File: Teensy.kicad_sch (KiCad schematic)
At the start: 8 parts

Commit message: test commit
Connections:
- net Servo_Pin1_1: now also Q100.24
- net Servo_Pin2_1: now also Q100.25
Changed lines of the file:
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@@
+	(wire
+		(pts
+			(xy 93.98 106.68) (xy 116.84 106.68)
+		)
+		(stroke
+			(width 0)
+			(type default)
+		)
+	)
 	(wire
 		(pts
@@
 		)
 		(stroke
+			(width 0)
+			(type default)
+		)
+	)
+	(wire
+		(pts
+			(xy 93.98 104.14) (xy 116.84 104.14)
+		)
+		(stroke

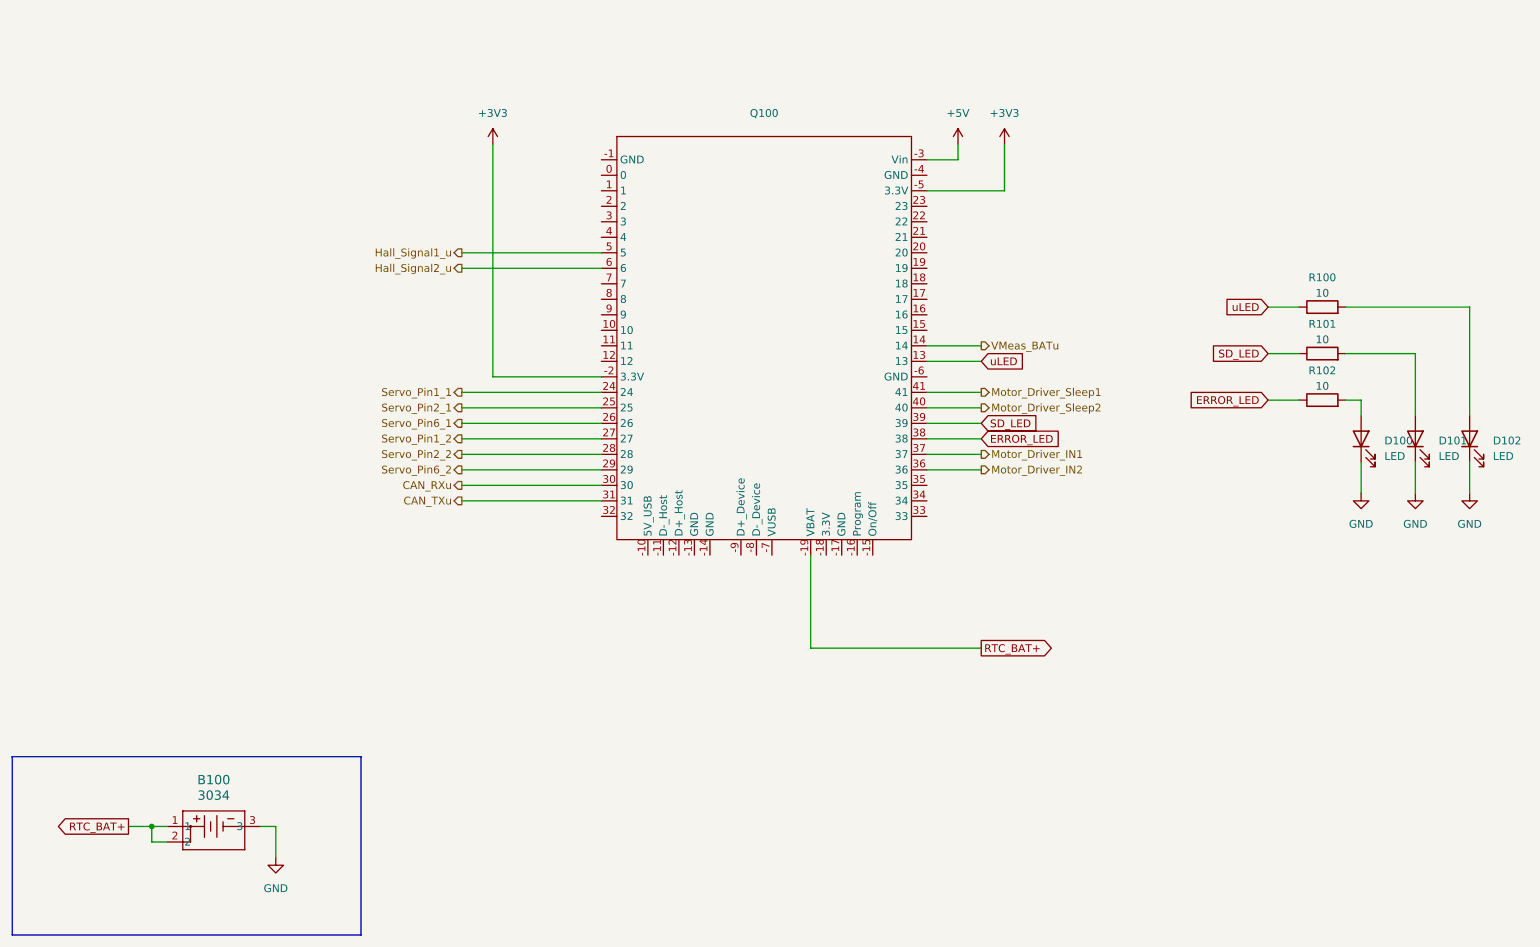
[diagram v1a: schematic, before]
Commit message: Added gyro, current sense, removed servo control, added temp sense
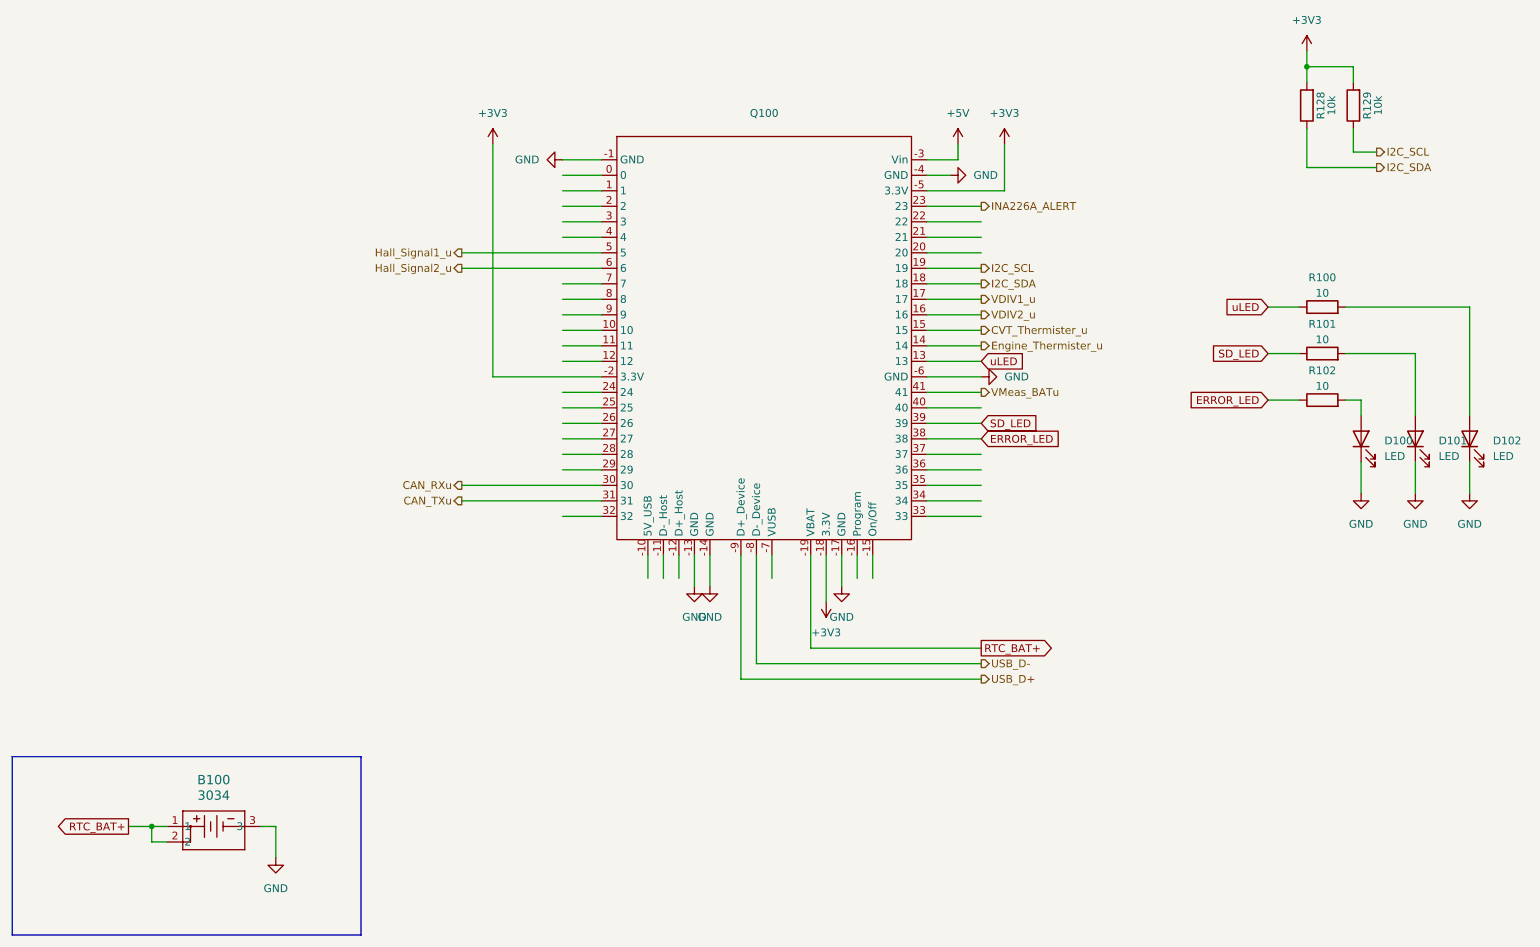
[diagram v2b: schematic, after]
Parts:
- added R128, R129: 10k, Resistor_SMD:R_0603_1608Metric_Pad0.98x0.95mm_HandSolder, symbol Device:R
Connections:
- net Motor_Driver_Sleep1 is gone; now on net VMeas_BATu: Q100.41
- net +3V3: now also Q100.-18 (3.3V), R128.2, R129.2
- net GND: now also Q100.-1 (GND), Q100.-13 (GND), Q100.-14 (GND), Q100.-17 (GND), Q100.-4 (GND), Q100.-6 (GND)
- net VMeas_BATu: no longer Q100.14
- net USB_D-: now reaches Q100.-8 (D-_Device)
- net USB_D+: now reaches Q100.-9 (D+_Device)
- net CVT_Thermister_u: now reaches Q100.15
- net VDIV2_u: now reaches Q100.16
- net VDIV1_u: now reaches Q100.17
- net I2C_SDA: now reaches Q100.18
- net I2C_SDA: now also R128.1
- net I2C_SCL: now reaches Q100.19
- net I2C_SCL: now also R129.1
- net INA226A_ALERT: now reaches Q100.23
- net Motor_Driver_IN1: no longer names the net of Q100.37
- net Motor_Driver_IN2: no longer names the net of Q100.36
- net Motor_Driver_Sleep2: no longer names the net of Q100.40
- net Servo_Pin1_1: no longer names the net of Q100.24
- net Servo_Pin1_2: no longer names the net of Q100.27
- net Servo_Pin2_1: no longer names the net of Q100.25
- net Servo_Pin2_2: no longer names the net of Q100.28
- net Servo_Pin6_1: no longer names the net of Q100.26
- net Servo_Pin6_2: no longer names the net of Q100.29
- new net Engine_Thermister_u: Q100.14

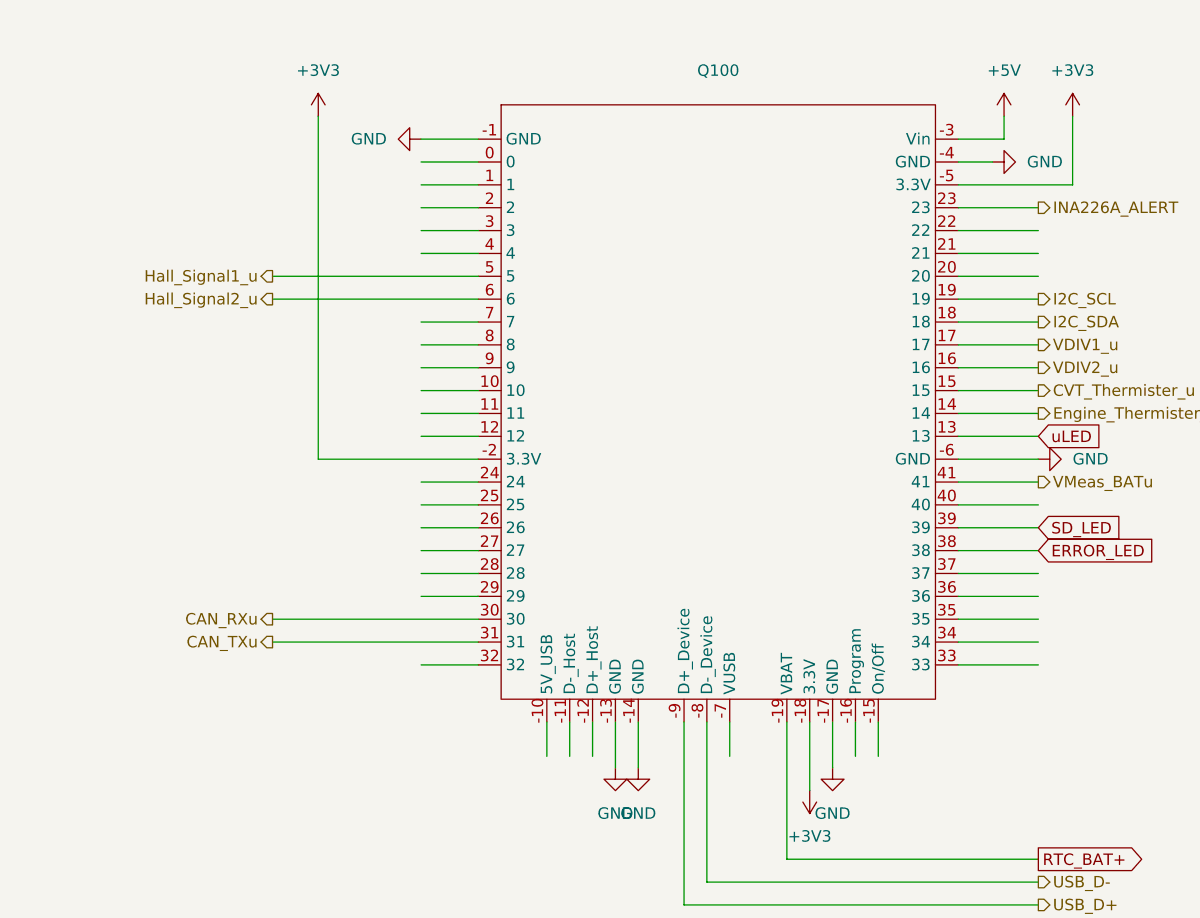
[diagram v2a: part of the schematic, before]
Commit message: finished up schematic, added magnetic sensor, cleaned up pins, etc.
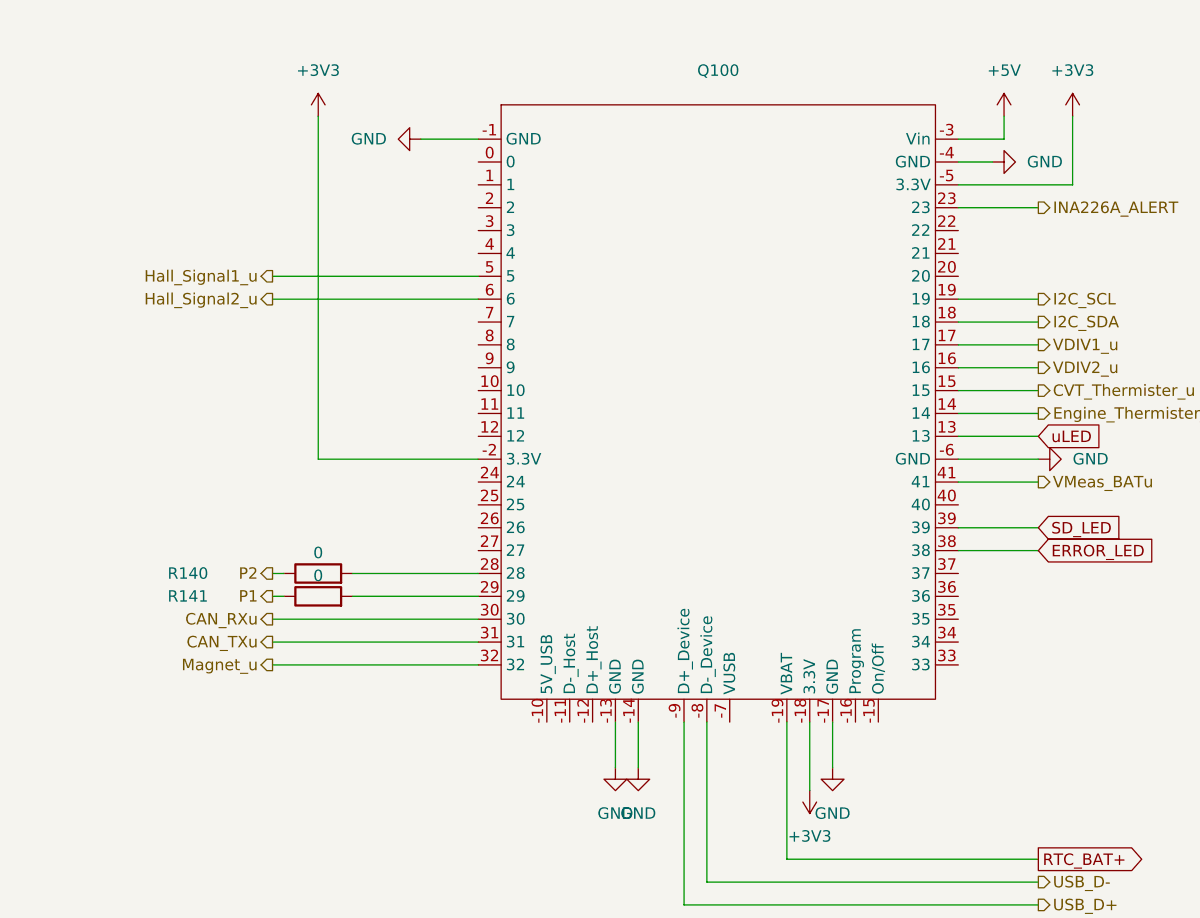
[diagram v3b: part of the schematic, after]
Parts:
- added R140, R141: 0, Resistor_SMD:R_0603_1608Metric_Pad0.98x0.95mm_HandSolder, symbol Device:R
- D100, D101, D102: footprint LED_SMD:LED_0805_2012Metric_Pad1.15x1.40mm_HandSolder -> LED_SMD:LED_0603_1608Metric_Pad1.05x0.95mm_HandSolder; Digikey https://www.digikey.com/en/products/detail/yongyu-optoelect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 -> (none)
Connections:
- net at Q100.28: now also R140.2
- net at Q100.29: now also R141.2
- net Magnet_u: now reaches Q100.32
- new net P1: R141.1
- new net P2: R140.1

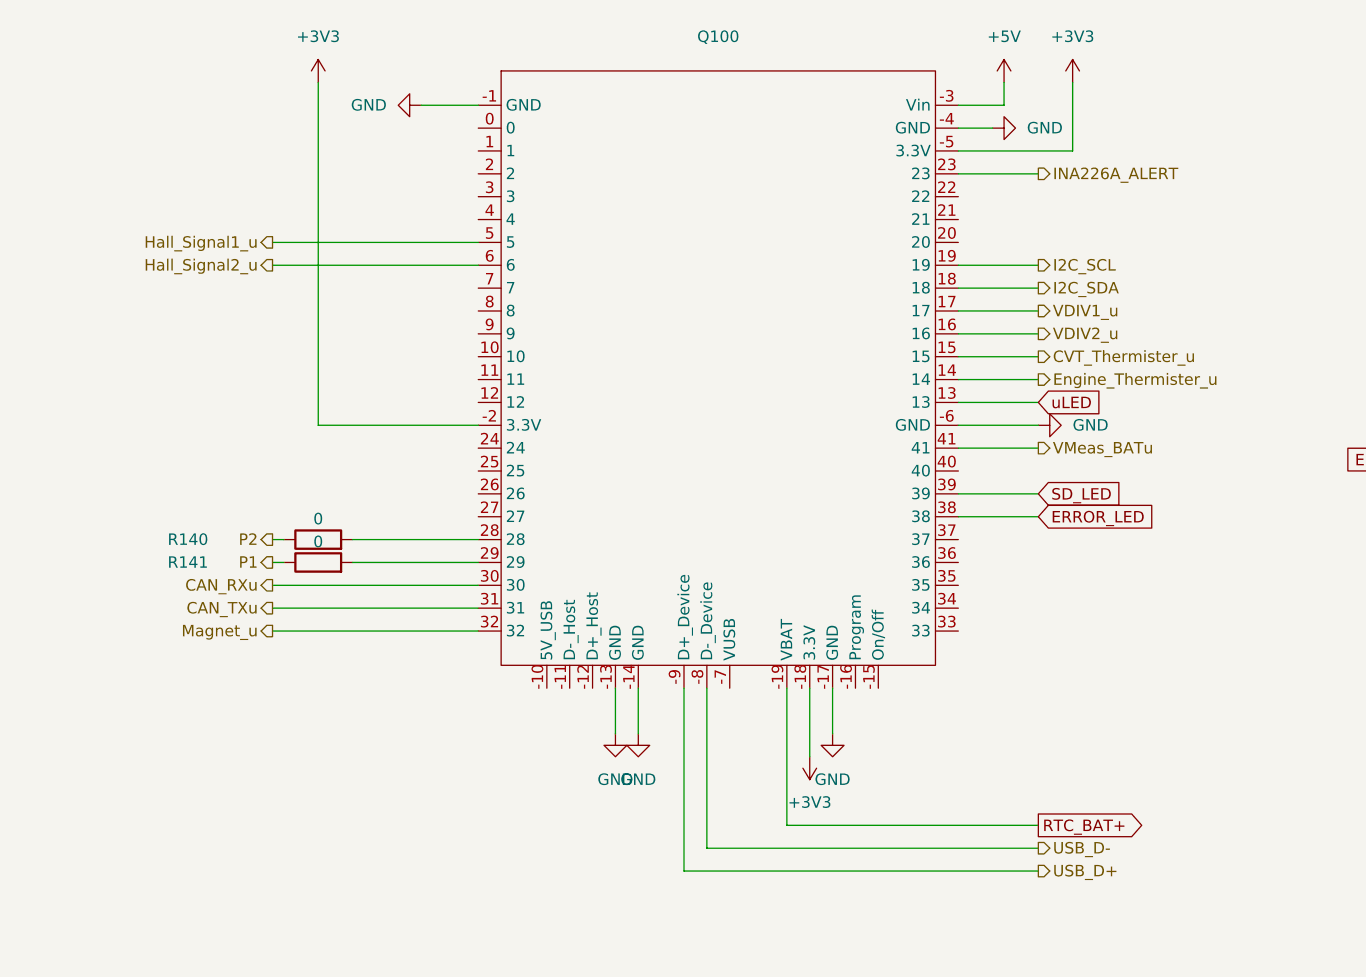
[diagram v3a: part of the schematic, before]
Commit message: final route. Needs revision and check of via placement.
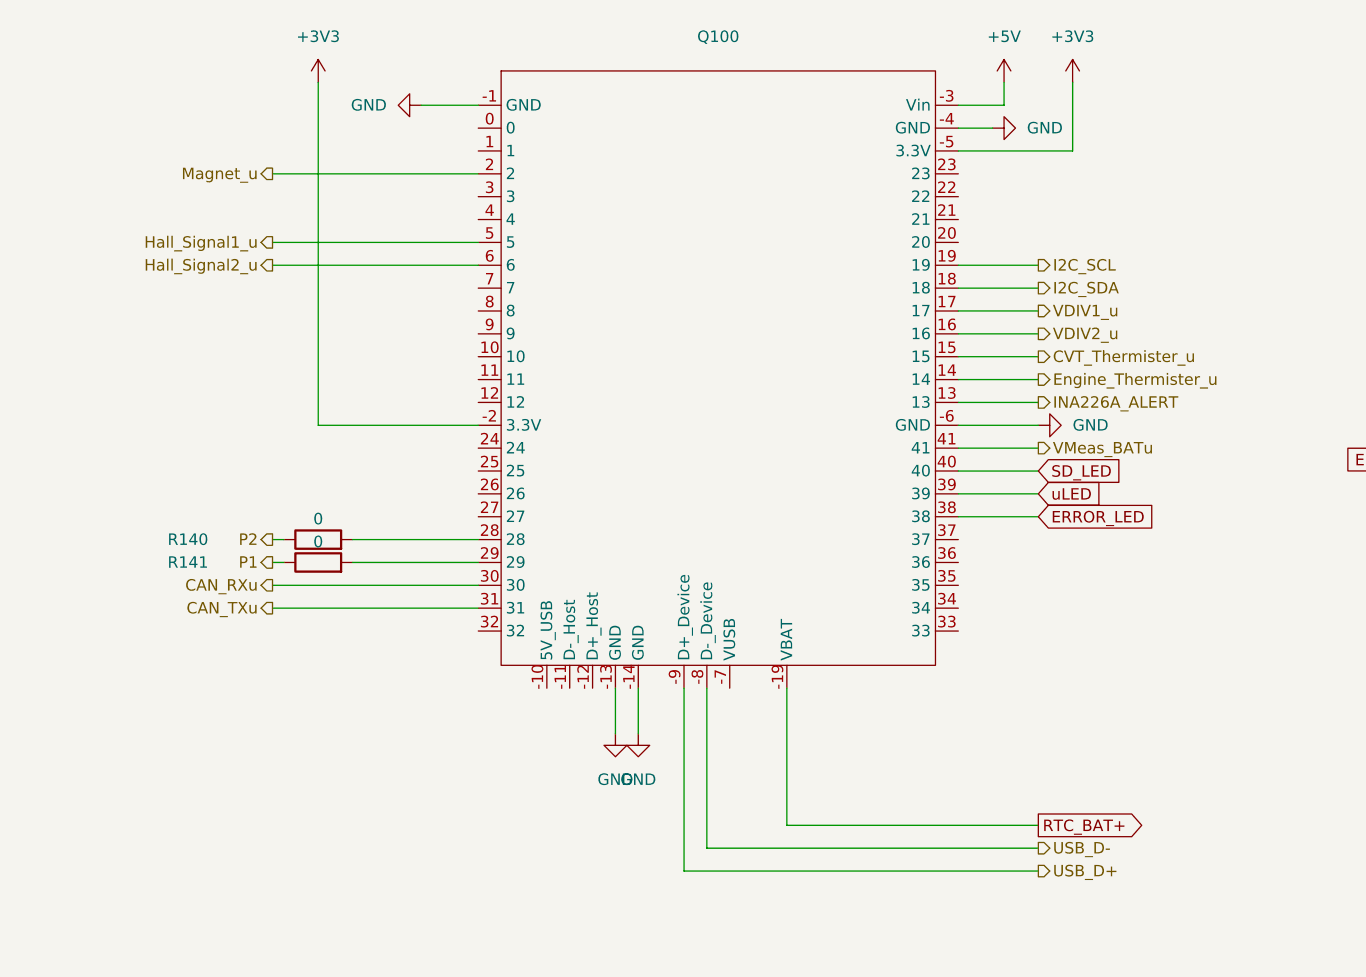
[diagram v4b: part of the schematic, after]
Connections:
- net +3V3: no longer Q100.-18 (3.3V)
- net GND: no longer Q100.-17 (GND)
- net INA226A_ALERT: now also Q100.13; no longer Q100.23
- net Magnet_u: now also Q100.2; no longer Q100.32
- net SD_LED: now also Q100.40; no longer Q100.39
- net uLED: now also Q100.39; no longer Q100.13

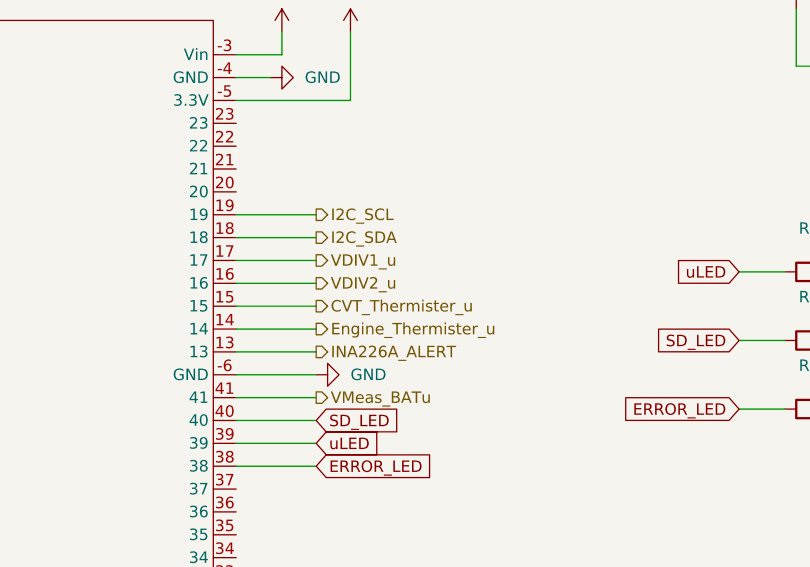
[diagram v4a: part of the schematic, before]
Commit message: removed a VDIV input and changed it to a thermistor input. Re-ran fabrication output
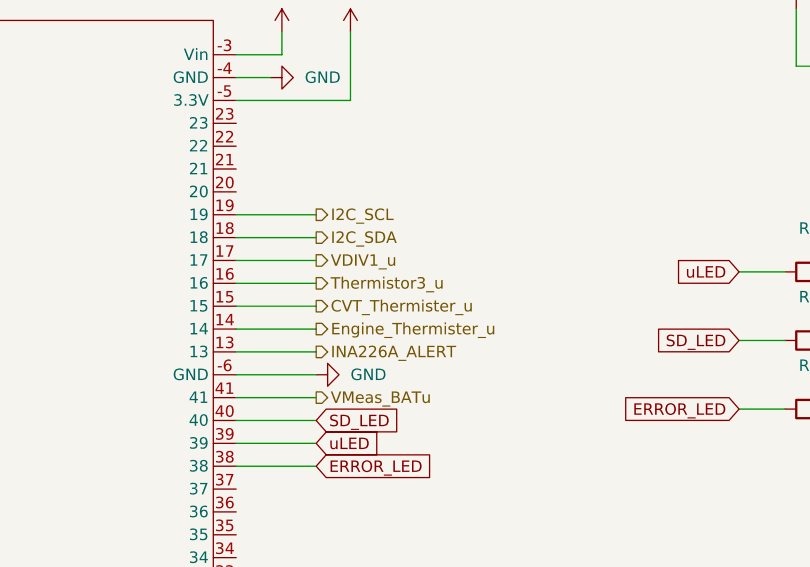
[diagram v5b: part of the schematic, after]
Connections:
- net VDIV2_u renamed Thermistor3_u
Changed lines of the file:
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@@
 		)
 	)
-	(hierarchical_label "VDIV2_u"
+	(hierarchical_label "Thermistor3_u"
 		(shape output)
 		(at 179.07 91.44 0)
